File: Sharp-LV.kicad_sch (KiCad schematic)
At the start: 35 parts, among them J1 USB_C_Receptacle_USB2.0, J2 Conn_01x05_PROG, U1 NRF52840-QIAA-R, U2 USBLC6-2P6, U3 MCP1700-3302E_SOT23, U4 RT9080-33GJ5, Y1 32.768K, Y2 32.768K

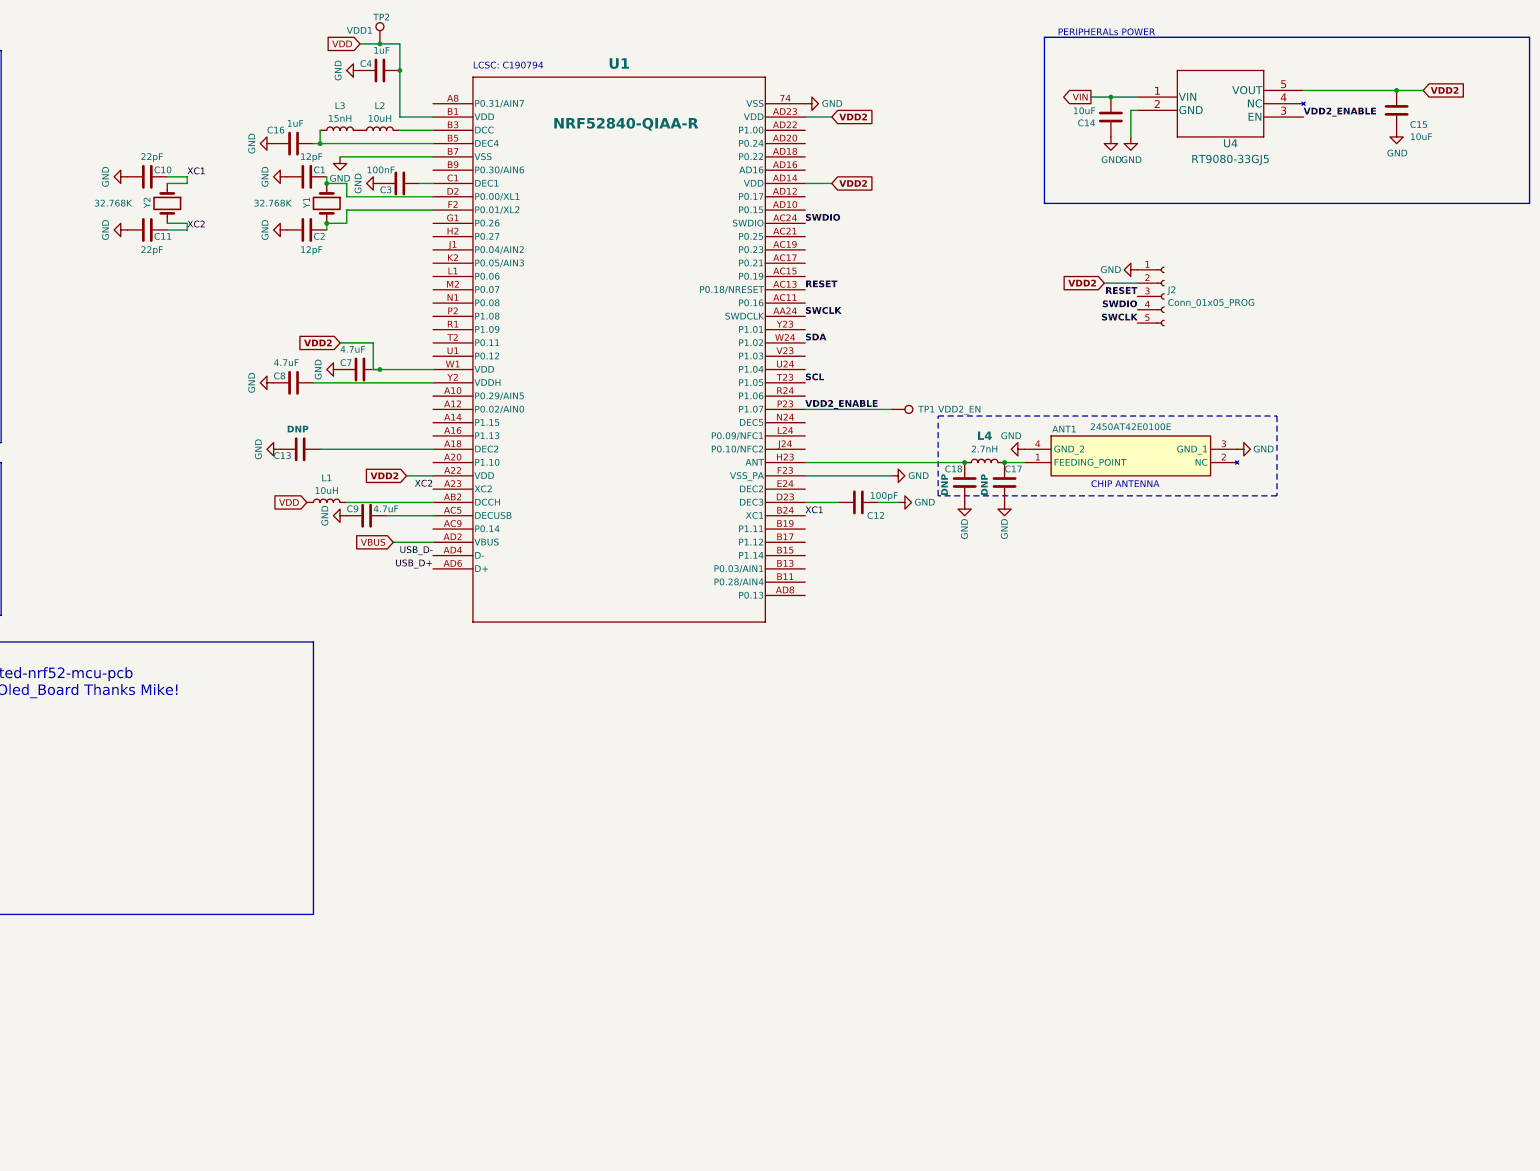
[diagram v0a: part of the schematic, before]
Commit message: 1.0 starting to take shape: Add LCD & touch CONN
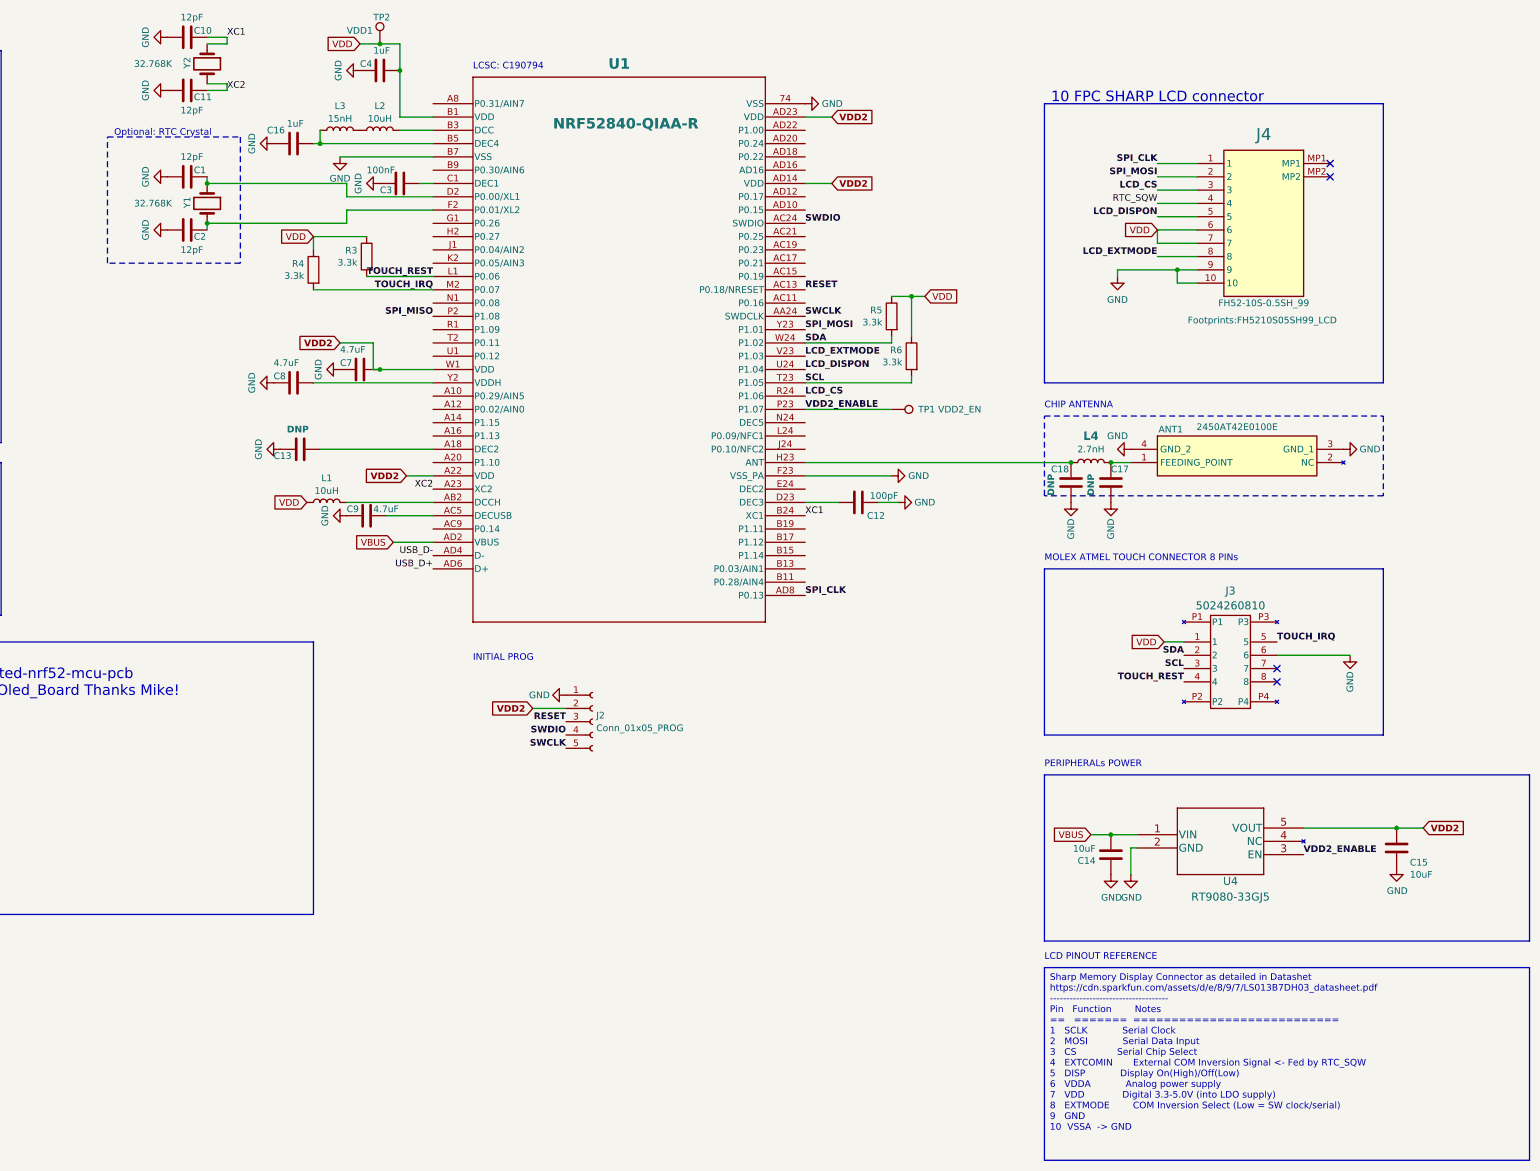
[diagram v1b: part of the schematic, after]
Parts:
- added J3: 5024260810, Footprints:CON_Molex_5024260812, symbol Molex:5024260812
- added J4: FH52-10S-0.5SH_99, Footprints:FH5210S05SH99_LCD, symbol 10_FPC:FH52-10S-0.5SH_99_
- added R3, R4, R5, R6: 3.3k, Resistor_SMD:R_0402_1005Metric, symbol Device:R
- C10, C11: value 22pF -> 12pF; LCSC C295968 -> C386126
- TP1: footprint TestPoint:TestPoint_Pad_D2.5mm -> TestPoint:TestPoint_Pad_D1.5mm
- TP2: footprint TestPoint:TestPoint_Pad_D2.5mm -> TestPoint:TestPoint_Pad_D1.0mm
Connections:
- net VIN is gone; now on net VBUS: C14.1, U4.1 (VIN)
- net GND: now also J3.6, J4.10, J4.9
- net SCL: now also J3.3, R6.2
- net SDA: now also J3.2, R5.2
- net VDD: now also J3.1, J4.6, J4.7, R3.1, R4.1, R5.1, R6.1
- net SPI_CLK: now reaches U1.AD8 (P0.13)
- net SPI_CLK: now also J4.1
- net TOUCH_REST: now reaches U1.L1 (P0.06)
- net TOUCH_REST: now also J3.4, R3.2
- net TOUCH_IRQ: now reaches U1.M2 (P0.07)
- net TOUCH_IRQ: now also J3.5, R4.2
- net SPI_MISO: now reaches U1.P2 (P1.08)
- net LCD_CS: now reaches U1.R24 (P1.06)
- net LCD_CS: now also J4.3
- net LCD_DISPON: now reaches U1.U24 (P1.04)
- net LCD_DISPON: now also J4.5
- net LCD_EXTMODE: now reaches U1.V23 (P1.03)
- net LCD_EXTMODE: now also J4.8
- net SPI_MOSI: now reaches U1.Y23 (P1.01)
- net SPI_MOSI: now also J4.2
- new net RTC_SQW: J4.4
- no-connect marks 2 -> 6
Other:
- note added: "10 FPC SHARP LCD connector"
- note added: "INITIAL PROG"
- note added: "LCD PINOUT REFERENCE"
- note added: "MOLEX ATMEL TOUCH CONNECTOR 8 PINs"
- note added: "Optional: RTC Crystal"
- moved on the sheet: ANT1, C1, C10, C11, C14, C15, C17, C18, C2, J2, L4, U4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

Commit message: Release 1.0 pending review
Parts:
- removed R1: 5.1k, Resistor_SMD:R_0603_1608Metric, symbol Device:R
- removed TP2: VDD1, TestPoint:TestPoint_Pad_D1.0mm, symbol Connector:TestPoint
- added BT1: Battery_Cell, Footprints:CoinBattery_MS621FE, symbol Device:Battery_Cell
- added C19: 820pF, Capacitor_SMD:C_0402_1005Metric, symbol Device:C
- added R7: 5.1k, Resistor_SMD:R_0603_1608Metric, symbol Device:R
- added Y3: RV-3032-C7, RV3032C7, symbol RTC:RV-3032-C7
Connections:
- net GND: now also BT1.2 (-), C19.2, R7.2, Y3.5 (VSS)
- net LCD_EXTMODE: now also U1.AD22 (P1.00); no longer U1.V23 (P1.03)
- net RTC_SQW: now also Y3.7 (CLKOUT)
- net SCL: now also Y3.8 (SCL)
- net SDA: now also R5.1, Y3.2 (SDA); no longer R5.2
- net TOUCH_IRQ: now also U1.N1 (P0.08); no longer U1.M2 (P0.07)
- net USB_D+: no longer J1.A6 (D+), J1.B6 (D+)
- net USB_D-: no longer J1.A7 (D-), J1.B7 (D-)
- net VDD: now also J2.3 (Pin_3), R5.2, Y3.6 (VDD); no longer R5.1
- net at U1.N24 (DEC5): now also C19.1
- net RESET: no longer names the net of U1.AC13 (P0.18/NRESET)
- net RESET: no longer J2.3 (Pin_3)
- net USB_U_D+ renamed USB_IN_D+
- net USB_IN_D+: now also J1.A6 (D+), J1.B6 (D+)
- net USB_U_D- renamed USB_IN_D-
- net USB_IN_D-: now also J1.A7 (D-), J1.B7 (D-)
- new net: R7.1, Y3.4 (EVI)
- new net RTC_INT: Y3.3 (~{INT})
- new net VDD_RTC: BT1.1 (+), Y3.1 (VBACKUP)
- no-connect marks 6 -> 34
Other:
- note added: "INITIAL PROG HEADER:"
- note added: "RTC SQW GENERATOR FOR LCD"
- note removed: "INITIAL PROG"
- moved on the sheet: J2, R3, R5, R6

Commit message: Revision 1.0 silk
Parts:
- added TP2: DEC2, symbol Connector:TestPoint
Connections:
- net at U1.E24 (DEC2): now also TP2.1
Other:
- note added: "No idea if we need this DEC2 circuit"

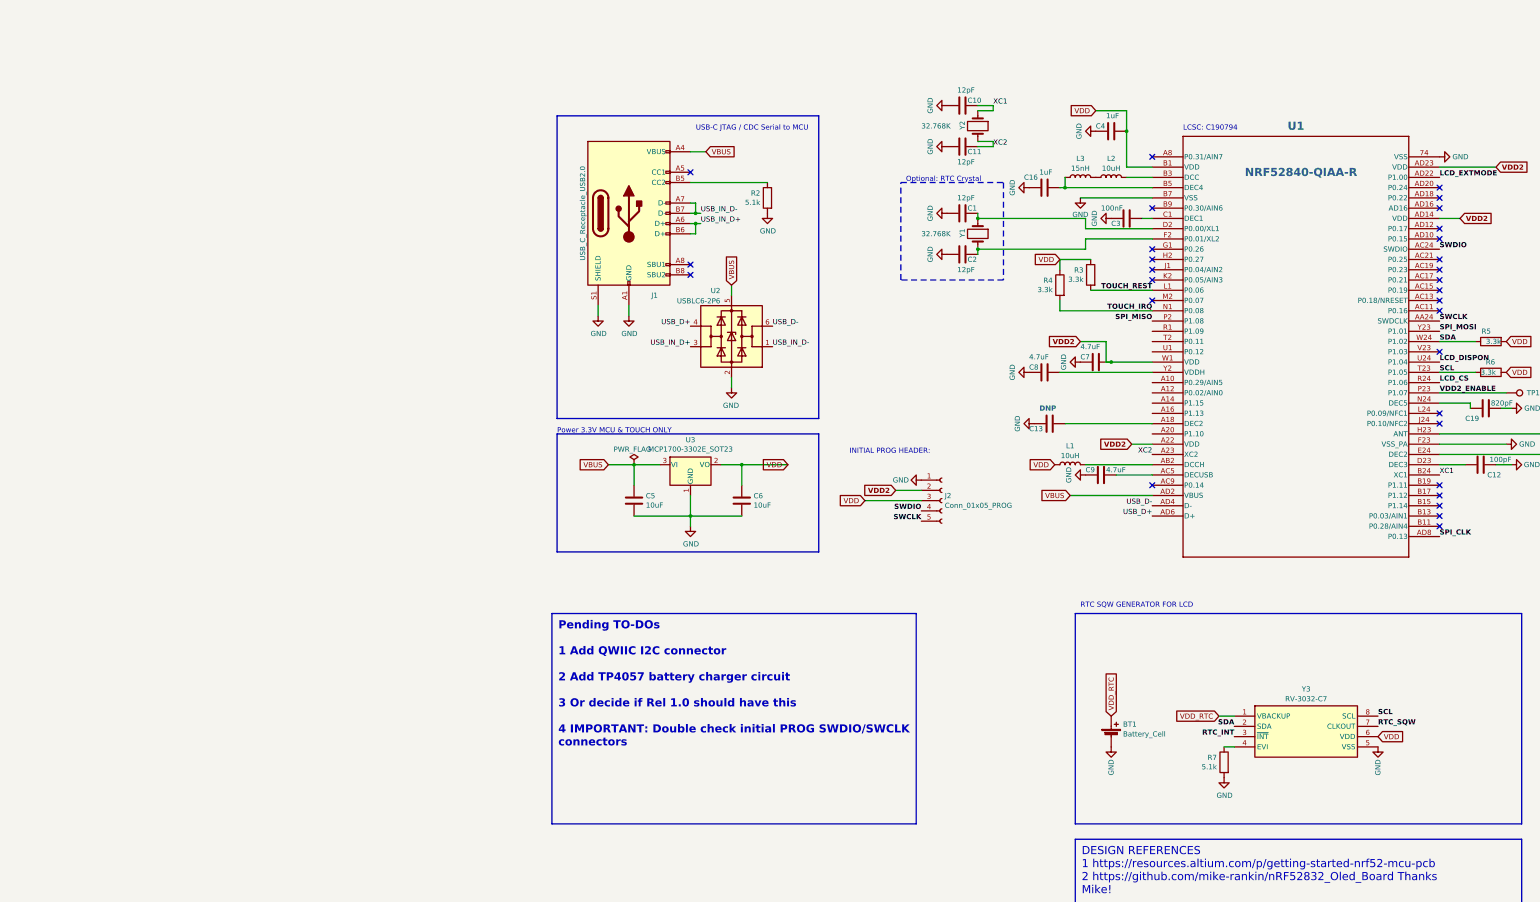
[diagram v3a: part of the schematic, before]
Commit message: Add QWIIC & headers
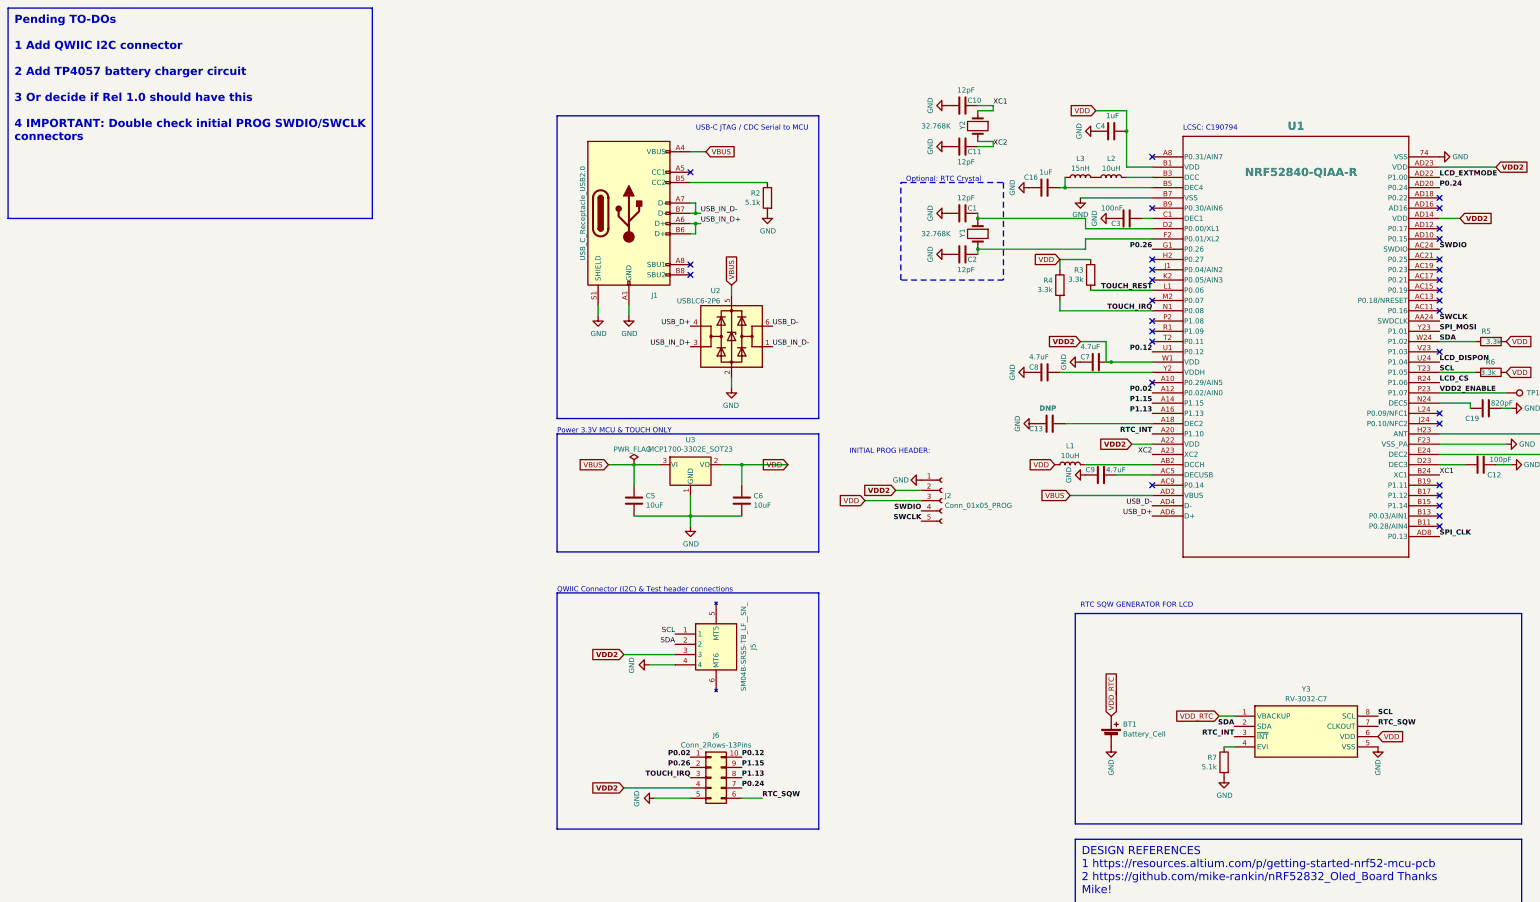
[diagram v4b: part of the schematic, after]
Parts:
- added J5: SM04B-SRSS-TB_LF__SN_, Footprints:QWIIC_SM04B-SRSS-TB_LFSN_, symbol Qwiic:SM04B-SRSS-TB_LF__SN_
- added J6: Conn_2Rows-13Pins, Connector_Samtec_HLE_SMD:Samtec_HLE-105-02-xxx-DV-A_2x05_P2.54mm_Horizontal, symbol Connector_Generic:Conn_02x05_Counter_Clockwise
- ANT1: Arrow Part Number 2450AT42E0100E -> (none); Arrow Price/Stock https://www.arrow.com/en/products/2450at42e0100e/johanson-d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 -> (none); LCSC (none) -> C3285081; Manufacturer_Part_Number 2450AT42E0100E -> (none); Mouser Part Number 609-2450AT42E0100E -> (none); Mouser Price/Stock https://www.mouser.co.uk/ProductDetail/Johanson-Technology/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 -> (none)
- J3: LCSC (none) -> C563931
- TP2: footprint (none) -> TestPoint:TestPoint_Pad_D1.0mm
- Y3: LCSC (none) -> C5127802
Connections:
- net GND: now also J5.4, J6.5 (Pin_5)
- net RTC_INT: now also U1.A20 (P1.10)
- net RTC_SQW: now also J6.6 (Pin_6)
- net SCL: now also J5.1
- net SDA: now also J5.2
- net TOUCH_IRQ: now also J6.3 (Pin_3)
- net VDD2: now also J5.3, J6.4 (Pin_4)
- net P0.02: now reaches U1.A12 (P0.02/AIN0)
- net P0.02: now also J6.1 (Pin_1)
- net P1.15: now reaches U1.A14 (P1.15)
- net P1.15: now also J6.9 (Pin_9)
- net P1.13: now reaches U1.A16 (P1.13)
- net P1.13: now also J6.8 (Pin_8)
- net P0.24: now reaches U1.AD20 (P0.24)
- net P0.24: now also J6.7 (Pin_7)
- net P0.26: now reaches U1.G1 (P0.26)
- net P0.26: now also J6.2 (Pin_2)
- net P0.12: now reaches U1.U1 (P0.12)
- net P0.12: now also J6.10 (Pin_10)
- net SPI_MISO: no longer names the net of U1.P2 (P1.08)
- no-connect marks 34 -> 36
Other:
- note added: "QWIIC Connector (I2C) & Test header connections"
